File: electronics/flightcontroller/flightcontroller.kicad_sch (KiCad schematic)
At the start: 13 parts, among them J2 ESC+, J3 ESC, J4 Servo3, J5 Servo2, J6 Servo1, J7 ESC-, SW1 SW_Push, U2 MPU-9250, U3 STM32F373RBTx

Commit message: electronics: Draft most of the flight controller schematics.
The power supply part is not complete, and all connections to the MCU are
missing.
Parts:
- removed SW1: SW_Push, Button_Switch_SMD:SW_SPST_CK_KXT3, symbol Switch:SW_Push
- removed U2: MPU-9250, Sensor_Motion:InvenSense_QFN-24_3x3mm_P0.4mm, symbol Sensor_Motion:MPU-9250
- removed U3: STM32F373RBTx, Package_QFP:LQFP-64_10x10mm_P0.5mm, symbol MCU_ST_STM32F3:STM32F373RBTx
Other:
- added sheet MCU (mcu.kicad_sch)
- added sheet Sensors (sensors.kicad_sch)
- note added: "TODO: - IMU - USB - NRF24L01 - Servo/battery connectors - Optional GPS - Altimeter/airspeed indicator? 2x Omron 2SMPB-02B (39-2SMPB-02BCT-ND) - Voltage regulator for servos (AOZ6663) and 3.3V (MIC5514) - SD card"
- note removed: "TODO: - IMU - USB - NRF24L01 - Servo/battery connectors - Optional GPS - Altimeter/airspeed indicator? 2x Omron 2SMPB-02B (39-2SMPB-02BCT-ND) - Voltage regulator for servos (AOZ6663) and 3.3V (MIC5514)"

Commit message: electronics: Changed the 4V regulator and added some ordering codes.
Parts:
- J3: Mouser (none) -> 474-PRT-10210
- J4, J5, J6: Digikey (none) -> 455-1803-1-ND

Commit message: PCB: USB, micro SD, and many component changes.
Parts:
- J4, J5, J6: footprint Connector_JST:JST_SH_SM03B-SRSS-TB_1x03-1MP_P1.00mm_Horizontal -> Connector_Molex:Molex_PicoBlade_53398-0371_1x03-1MP_P1.25mm_Vertical; Digikey 455-1803-1-ND -> (none); Mouser (none) -> 538-53398-0376

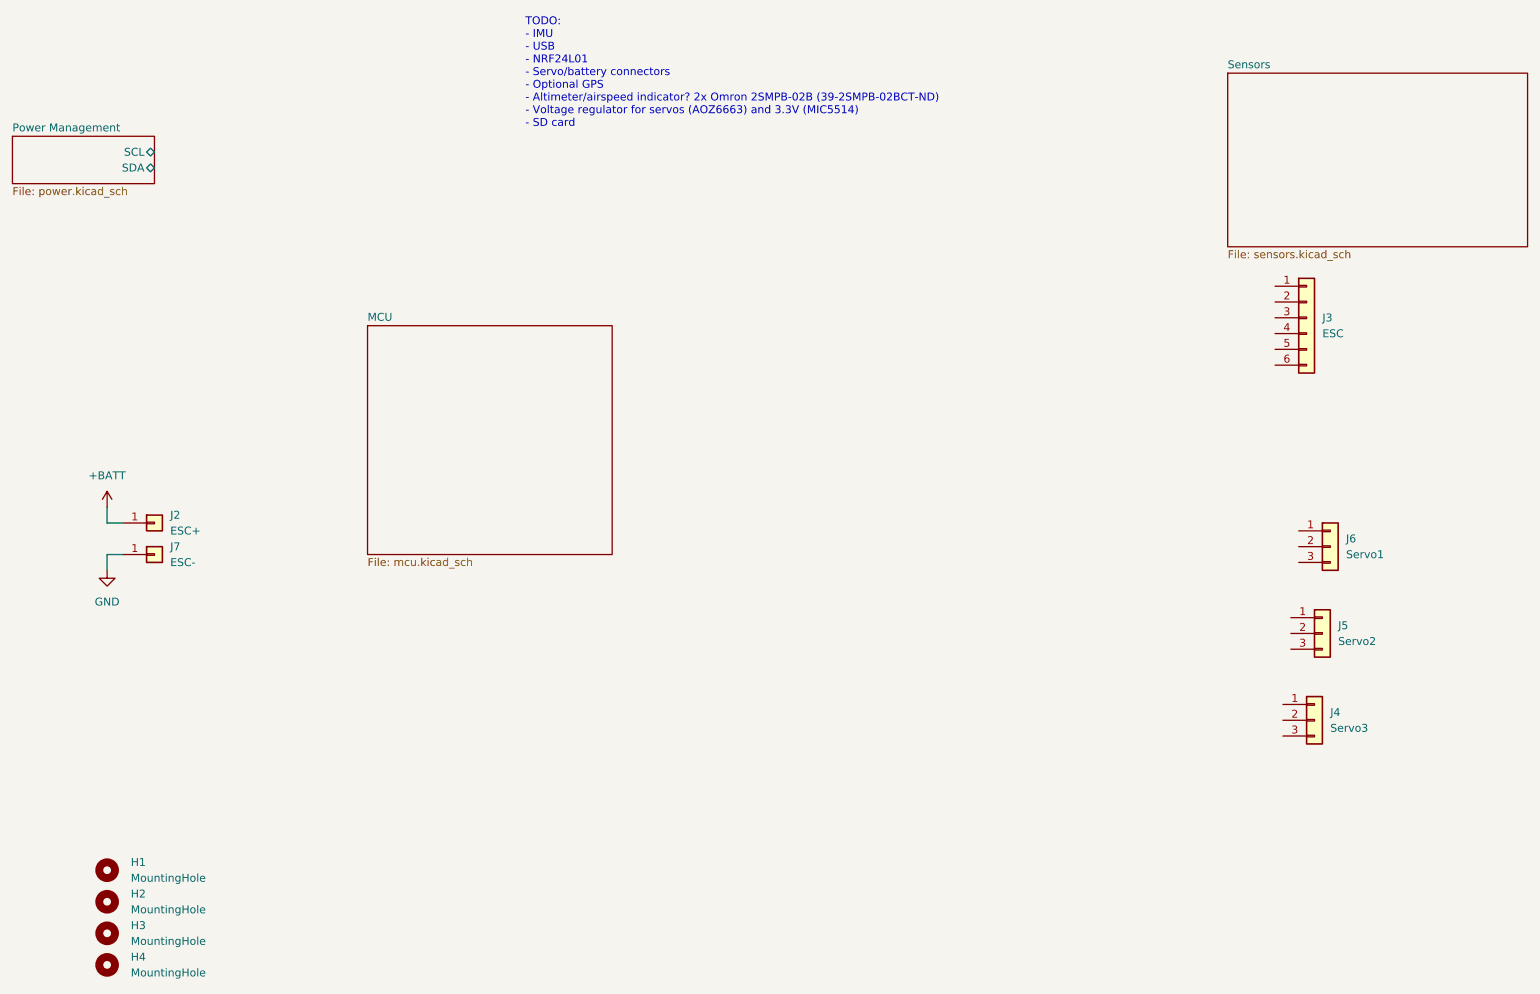
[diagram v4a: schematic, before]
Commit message: electronics: Microcontroller connections, general component placement.
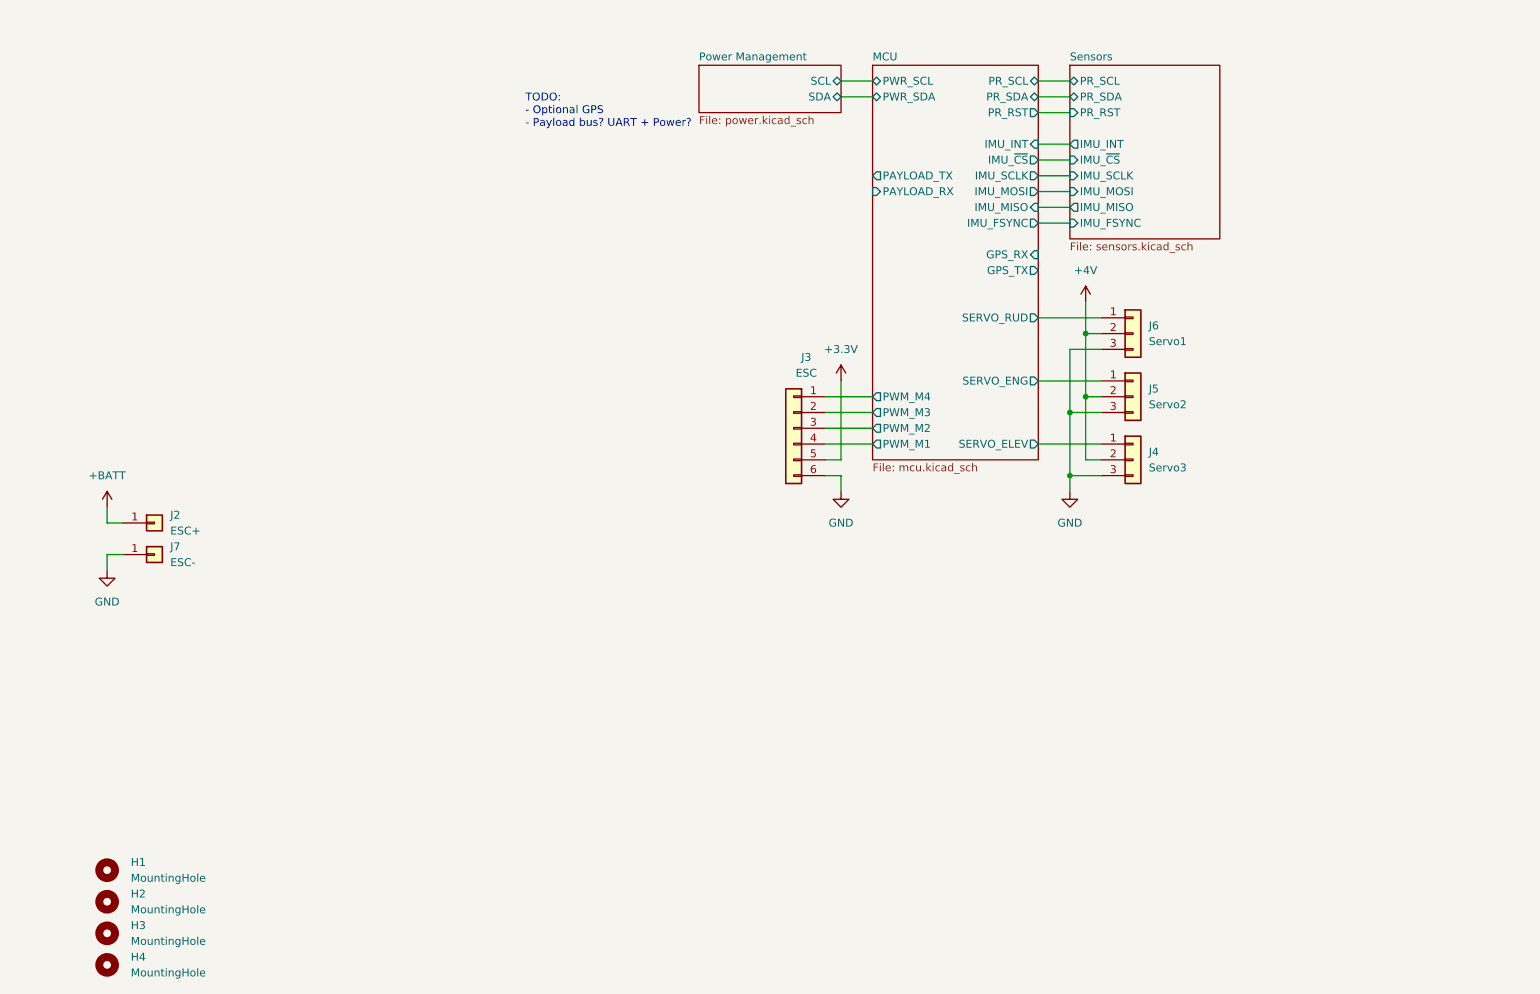
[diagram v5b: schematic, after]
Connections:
- net GND: now also J3.6 (Pin_6), J4.3 (Pin_3), J5.3 (Pin_3), J6.3 (Pin_3)
- net MCU/SERVO_RUD: now reaches J6.1 (Pin_1)
- net +4V: now reaches J6.2 (Pin_2)
- net +4V: now also J4.2 (Pin_2), J5.2 (Pin_2)
- net MCU/SERVO_ELEV: now reaches J4.1 (Pin_1)
- net MCU/PWM_M4: now reaches J3.1 (Pin_1)
- net MCU/PWM_M3: now reaches J3.2 (Pin_2)
- net MCU/PWM_M2: now reaches J3.3 (Pin_3)
- net MCU/PWM_M1: now reaches J3.4 (Pin_4)
- net +3V3: now reaches J3.5 (Pin_5)
- net MCU/SERVO_ENG: now reaches J5.1 (Pin_1)
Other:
- sheet MCU ports: added GPS_RX, GPS_TX, IMU_FSYNC, IMU_INT, IMU_MISO, IMU_MOSI, IMU_SCLK, IMU_~{CS}, PAYLOAD_RX, PAYLOAD_TX, PR_RST, PR_SCL, PR_SDA, PWM_M1, PWM_M2, PWM_M3, PWM_M4, PWR_SCL, PWR_SDA, SERVO_ELEV, SERVO_ENG, SERVO_RUD; removed none
- sheet Sensors ports: added IMU_FSYNC, IMU_INT, IMU_MISO, IMU_MOSI, IMU_SCLK, IMU_~{CS}, PR_RST, PR_SCL, PR_SDA; removed none
- note added: "TODO: - Optional GPS - Payload bus? UART + Power?"
- note removed: "TODO: - IMU - USB - NRF24L01 - Servo/battery connectors - Optional GPS - Altimeter/airspeed indicator? 2x Omron 2SMPB-02B (39-2SMPB-02BCT-ND) - Voltage regulator for servos (AOZ6663) and 3.3V (MIC5514) - SD card"
- moved on the sheet: J3, J4, J5, J6

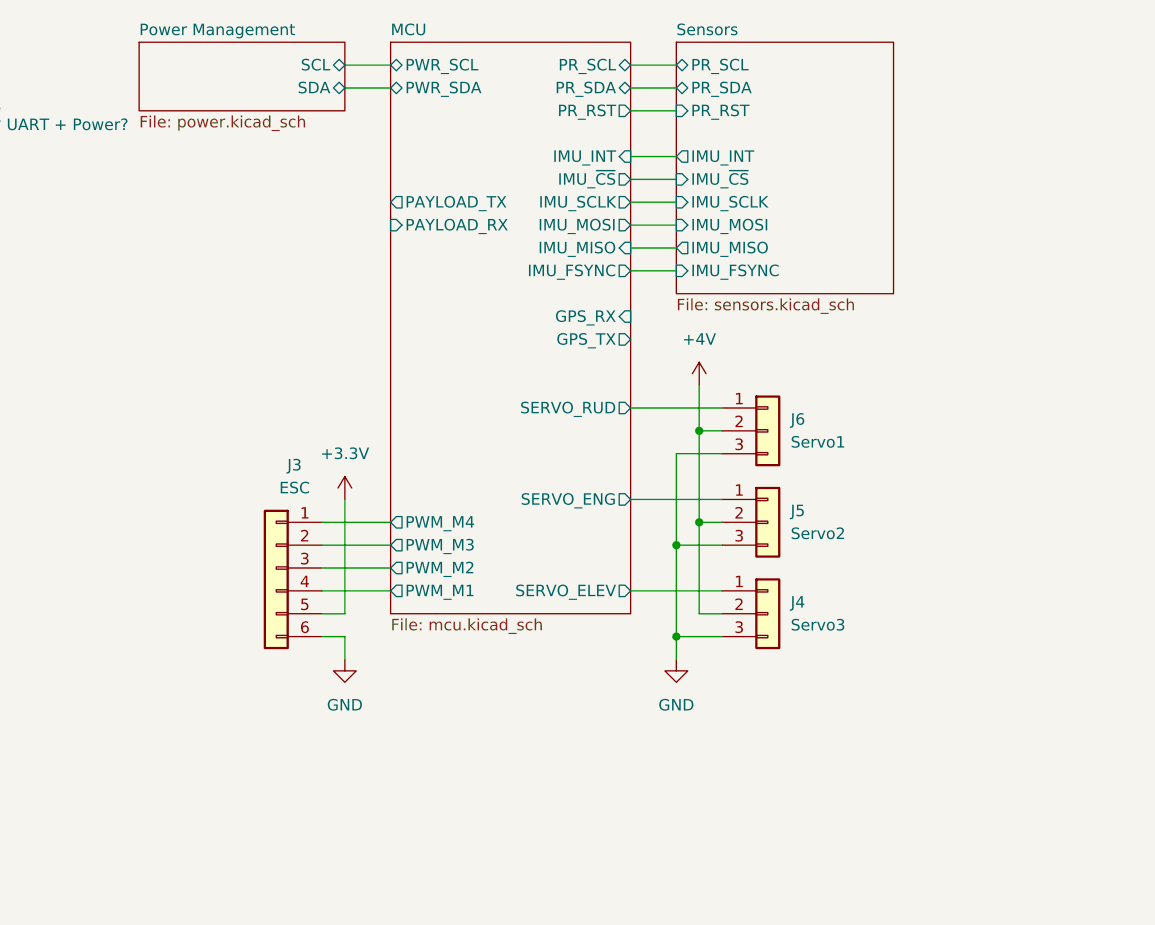
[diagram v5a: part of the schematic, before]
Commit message: electronics: Fix remaining schematics ERC errors.
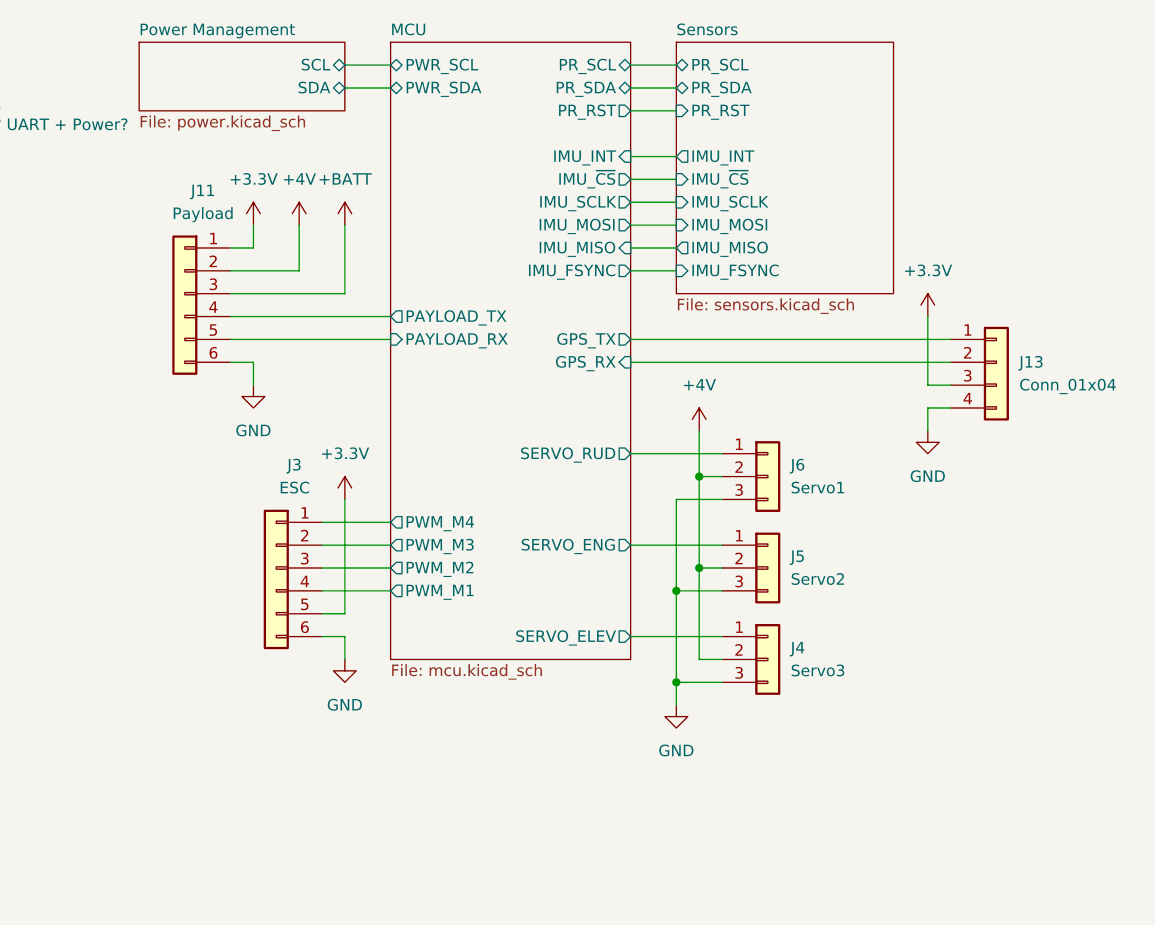
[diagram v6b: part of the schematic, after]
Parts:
- added J11: Payload, Connector_JST:JST_SH_SM06B-SRSS-TB_1x06-1MP_P1.00mm_Horizontal, symbol Connector_Generic:Conn_01x06
- added J13: Conn_01x04, Connector_Molex:Molex_PicoBlade_53398-0471_1x04-1MP_P1.25mm_Vertical, symbol Connector_Generic:Conn_01x04
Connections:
- net +3V3: now also J11.1 (Pin_1), J13.3 (Pin_3)
- net +4V: now also J11.2 (Pin_2)
- net +BATT: now also J11.3 (Pin_3)
- net GND: now also J11.6 (Pin_6), J13.4 (Pin_4)
- net MCU/GPS_RX: now also J13.2 (Pin_2)
- net MCU/GPS_TX: now also J13.1 (Pin_1)
- net MCU/PAYLOAD_RX: now also J11.5 (Pin_5)
- net MCU/PAYLOAD_TX: now also J11.4 (Pin_4)
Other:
- moved on the sheet: J4, J5, J6

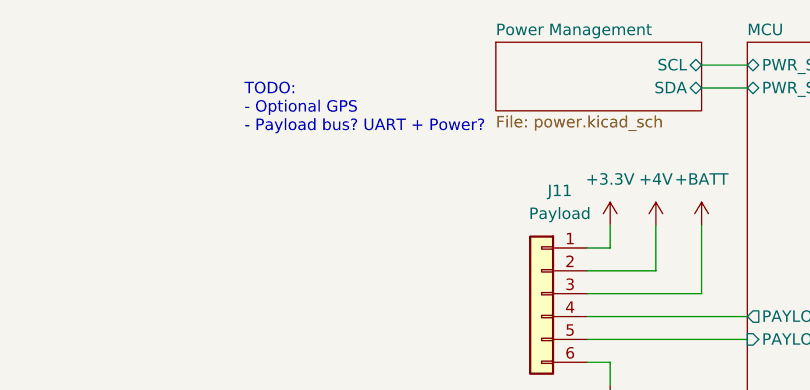
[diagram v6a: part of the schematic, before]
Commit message: electronics: Fixed the reset switch footprint.
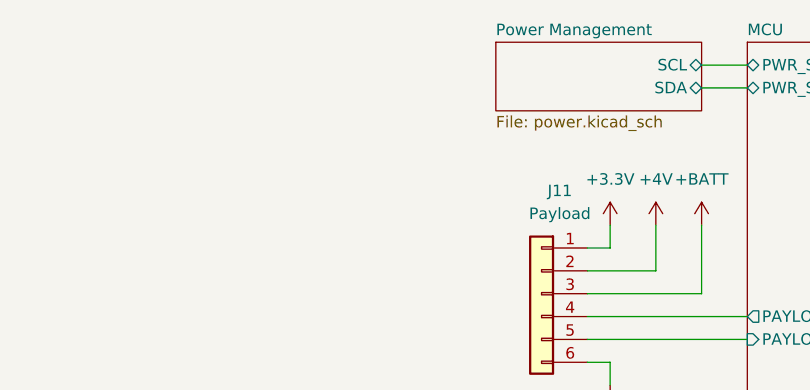
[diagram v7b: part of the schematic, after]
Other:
- note removed: "TODO: - Optional GPS - Payload bus? UART + Power?"
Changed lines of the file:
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@@
     (stroke (width 0) (type solid) (color 0 0 0 0))
-  )
-  (text "TODO:\n- Optional GPS\n- Payload bus? UART + Power?" (at 106.68 30.48 0)
-    (effects (font (size 1.27 1.27)) (justify left bottom))
   )
   (symbol (lib_id "power:+BATT") (at 39.37 91.44 0) (unit 1)
@@
     )
     (path "/9e22fcca-13c3-4897-835c-f83365def6e5/719a0b0c-6071-4ff4-af80-4a3792d2d8c0"
-      (reference "SW1") (unit 1) (value "RESET") (footprint "Button_Switch_SMD:SW_SPST_CK_KXT3")
+      (reference "SW1") (unit 1) (value "RESET") (footprint "flightcontroller-footprints:SW_SPST_PTS815")
     )
     (path "/035be36c-3be5-4834-b928-6ed73ad80857/f0e50344-1b2a-43a9-a48f-bb9e18ff0cfb"

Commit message: electronics: Finished wiring of the flight controller PCB.
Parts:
- J11, J3: symbol Connector_Generic:Conn_01x06 -> Connector_Generic_MountingPin:Conn_01x06_MountingPin
- J13: symbol Connector_Generic:Conn_01x04 -> Connector_Generic_MountingPin:Conn_01x04_MountingPin
- J4, J5, J6: symbol Connector_Generic:Conn_01x03 -> Connector_Generic_MountingPin:Conn_01x03_MountingPin
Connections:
- net GND: now also J11.MP (MountPin), J13.MP (MountPin), J3.MP (MountPin), J4.MP (MountPin), J5.MP (MountPin), J6.MP (MountPin)
